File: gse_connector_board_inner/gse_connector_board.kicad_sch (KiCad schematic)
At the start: 27 parts, among them J1 arming_connector, J2 gse_com_connector, J3 chg_connector, J4 Conn_02x03_Top_Bottom, J5 Conn_02x02_Top_Bottom, U7 ISO1044BD, U9 MCP2562-E-SN

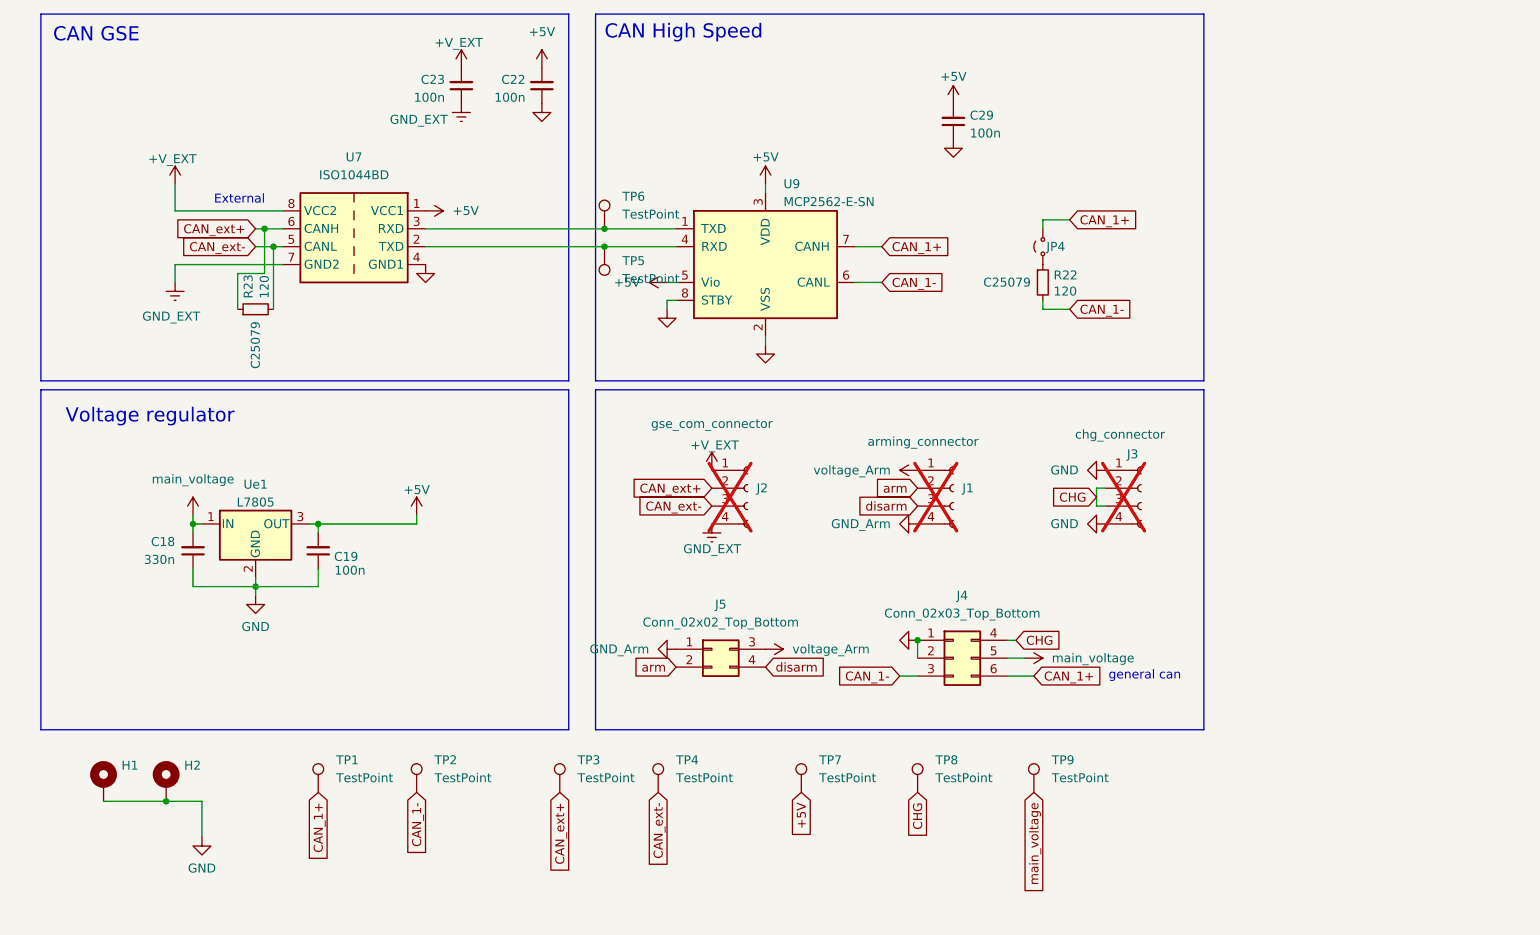
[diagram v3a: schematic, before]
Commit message: replace can isolation with mosfet
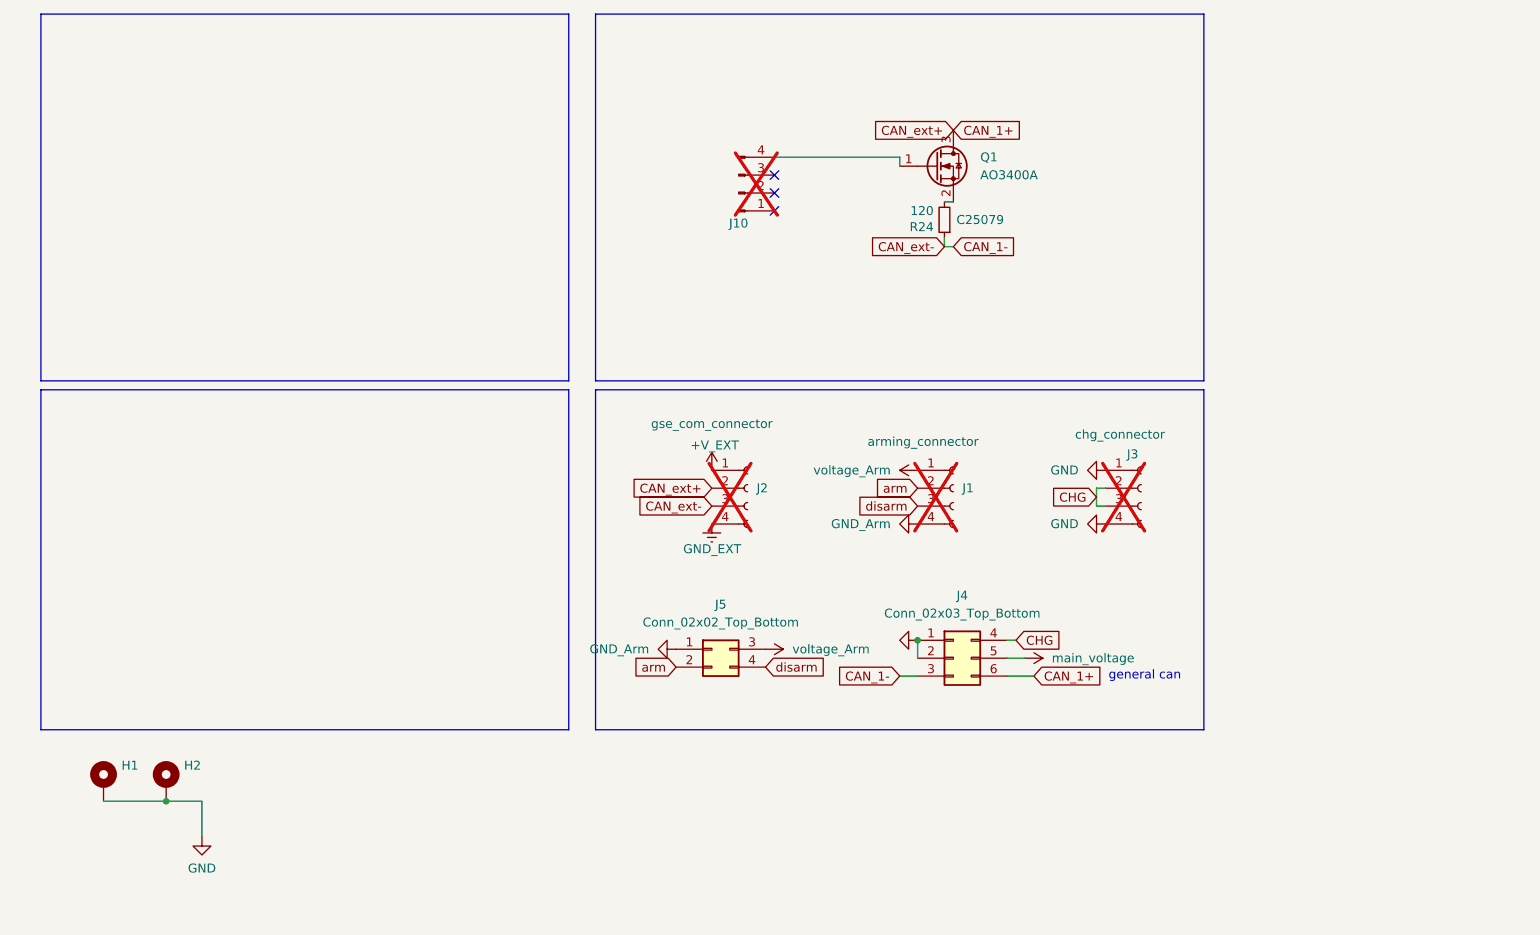
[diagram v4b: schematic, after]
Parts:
- removed C18: 330n, Capacitor_SMD:C_0603_1608Metric, symbol Device:C_Small
- removed C19: 100n, Capacitor_SMD:C_0603_1608Metric, symbol Device:C_Small
- removed C22, C23, C29: 100n, Capacitor_SMD:C_0603_1608Metric_Pad1.08x0.95mm_HandSolder, symbol Device:C_Small
- removed JP4: Jumper_2_Small_Open, Jumper:SolderJumper-2_P1.3mm_Bridged_RoundedPad1.0x1.5mm, symbol Jumper:Jumper_2_Small_Open
- removed R22, R23: 120, Resistor_SMD:R_0402_1005Metric, symbol Device:R_Small
- removed TP1, TP2, TP3, TP4, TP5, TP6, TP7, TP8, TP9: TestPoint, TestPoint:TestPoint_Pad_D1.5mm, symbol Connector:TestPoint
- removed U7: ISO1044BD, Package_SO:SOIC-8_3.9x4.9mm_P1.27mm, symbol Interface_CAN_LIN:ISO1044BD
- removed U9: MCP2562-E-SN, Package_SO:SOIC-8_3.9x4.9mm_P1.27mm, symbol Interface_CAN_LIN:MCP2562-E-SN
- removed Ue1: L7805, Package_TO_SOT_SMD:TO-252-2, symbol Regulator_Linear:L7805
- added J10: JST-GH 4Pin, Connector_JST:JST_GH_BM04B-GHS-TBT_1x04-1MP_P1.25mm_Vertical, symbol Connector:Conn_01x04_Pin
- added Q1: AO3400A, Package_TO_SOT_SMD:SOT-23, symbol Transistor_FET:AO3400A
- added R24: 120, Resistor_SMD:R_0402_1005Metric, symbol Device:R_Small
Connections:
- net CAN_ext+ is gone; now on net CAN_1+: J2.2 (Pin_2)
- net CAN_ext- is gone; now on net CAN_1-: J2.3 (Pin_3)
- net CAN_1+: now also Q1.3 (D)
- net CAN_1-: now also R24.1
- new net: Q1.2 (S), R24.2
- new net: J10.4 (Pin_4), Q1.1 (G)
- no-connect marks 0 -> 3
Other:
- note removed: "CAN GSE"
- note removed: "CAN High Speed"
- note removed: "External"
- note removed: "Voltage regulator"

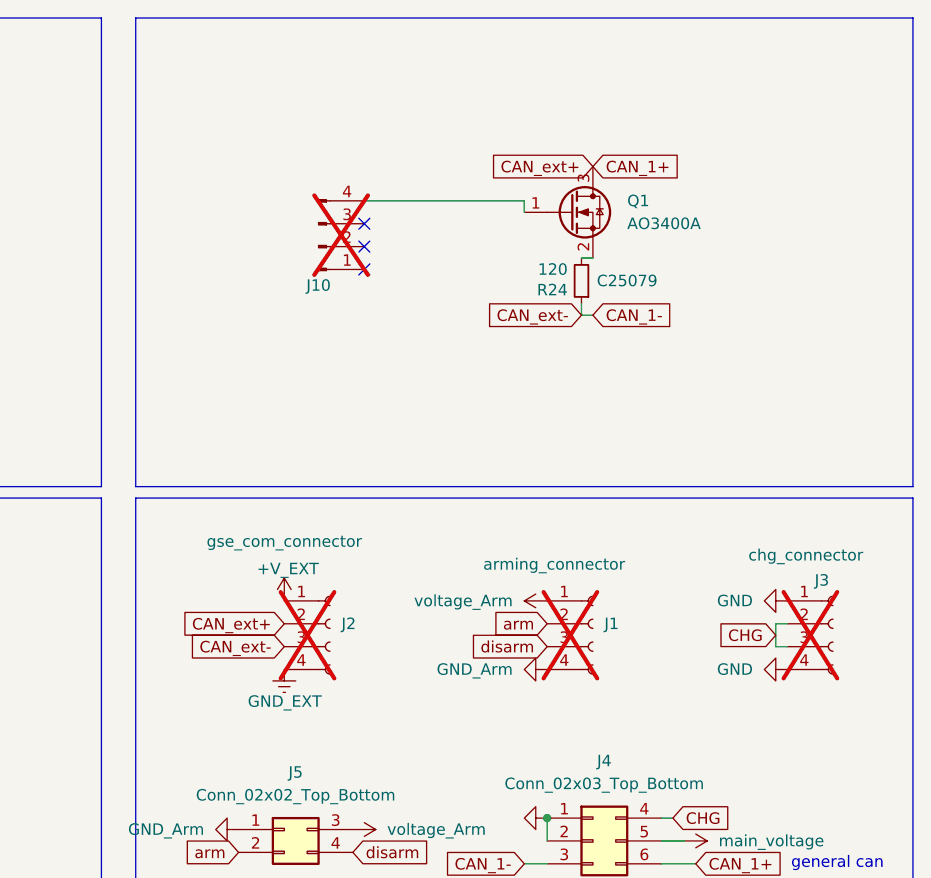
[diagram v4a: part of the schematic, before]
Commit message: replace can isolation with würth part
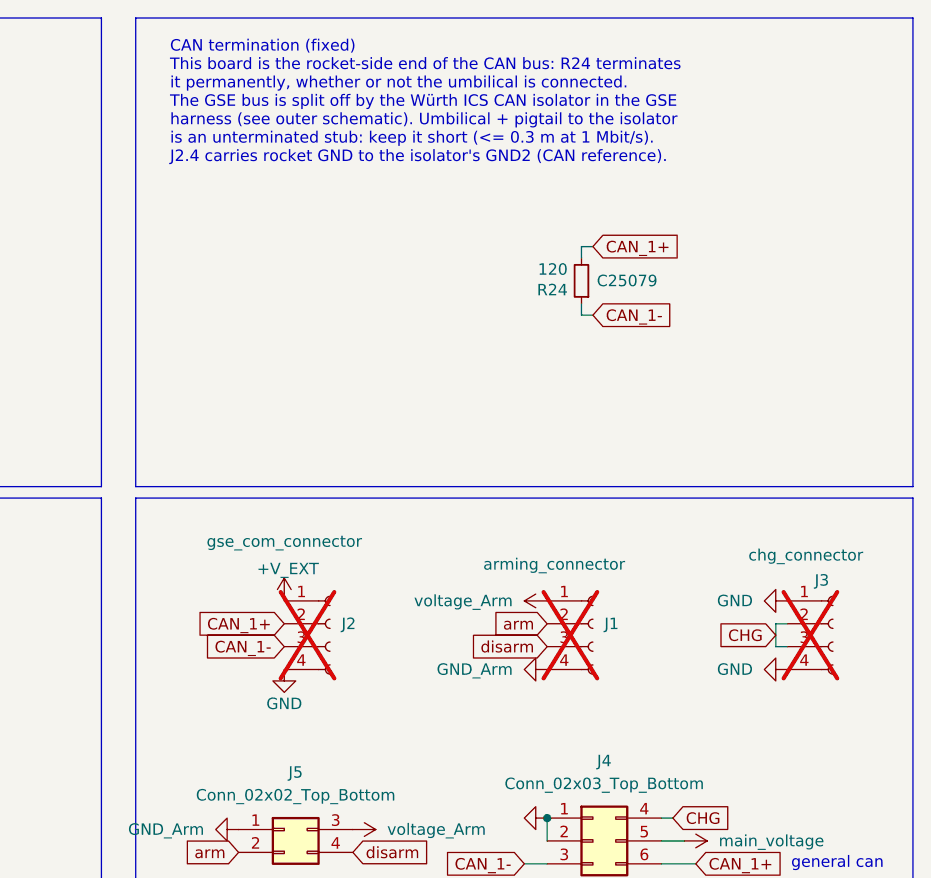
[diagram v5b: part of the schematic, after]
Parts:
- removed J10: JST-GH 4Pin, Connector_JST:JST_GH_BM04B-GHS-TBT_1x04-1MP_P1.25mm_Vertical, symbol Connector:Conn_01x04_Pin
- removed Q1: AO3400A, Package_TO_SOT_SMD:SOT-23, symbol Transistor_FET:AO3400A
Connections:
- net GND_EXT is gone; now on net GND: J2.4 (Pin_4)
- net CAN_1+: now also R24.2
- no-connect marks 3 -> 0
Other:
- note added: "CAN termination (fixed) This board is the rocket-side end of the CAN bus: R24 terminates it permanently, whether or not the umbilical is connected. The GSE bus is split off by the Würth ICS CAN isolator in the GSE harness (see outer schematic). Umbilical + pigtail to the isolator is an unterminated stub: keep it short (<= 0.3 m at 1 Mbit/s). J2.4 carries rocket GND to the isolator's GND2 (CAN ref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"

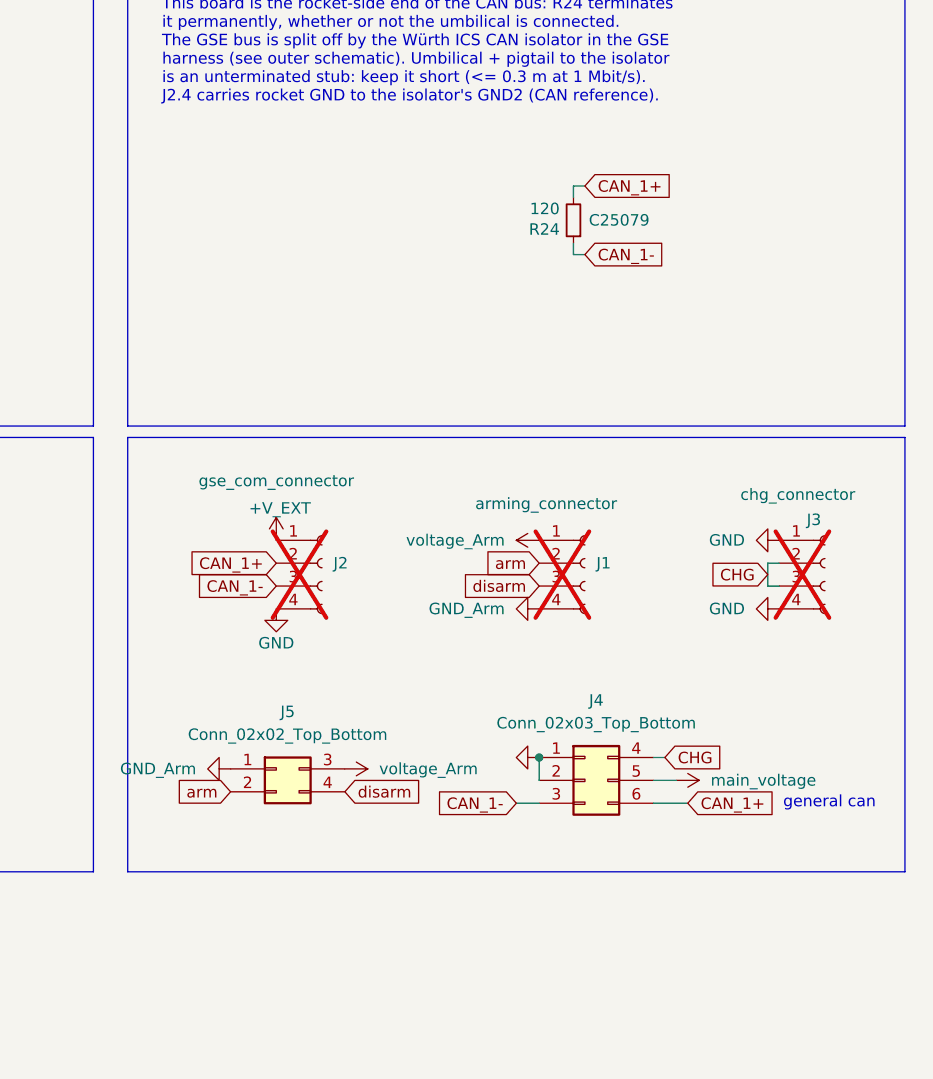
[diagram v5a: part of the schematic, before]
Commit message: add esd protection
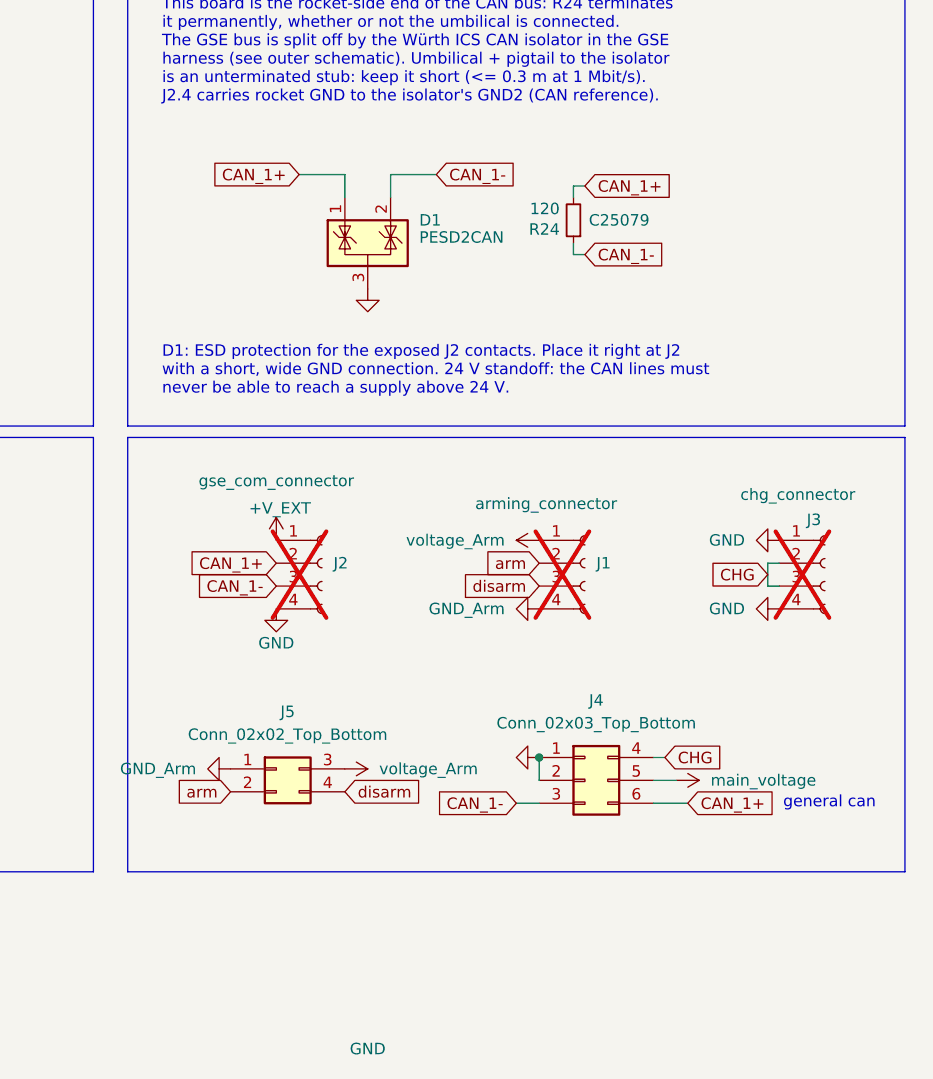
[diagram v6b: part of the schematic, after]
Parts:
- added D1: PESD2CAN, Package_TO_SOT_SMD:SOT-23, symbol Power_Protection:NUP2105L
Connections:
- net CAN_1+: now also D1.1 (K)
- net CAN_1-: now also D1.2 (K)
- net GND: now also D1.3 (A)
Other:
- note added: "D1: ESD protection for the exposed J2 contacts. Place it right at J2 with a short, wide GND connection. 24 V standoff: the CAN lines must never be able to reach a supply above 24 V."

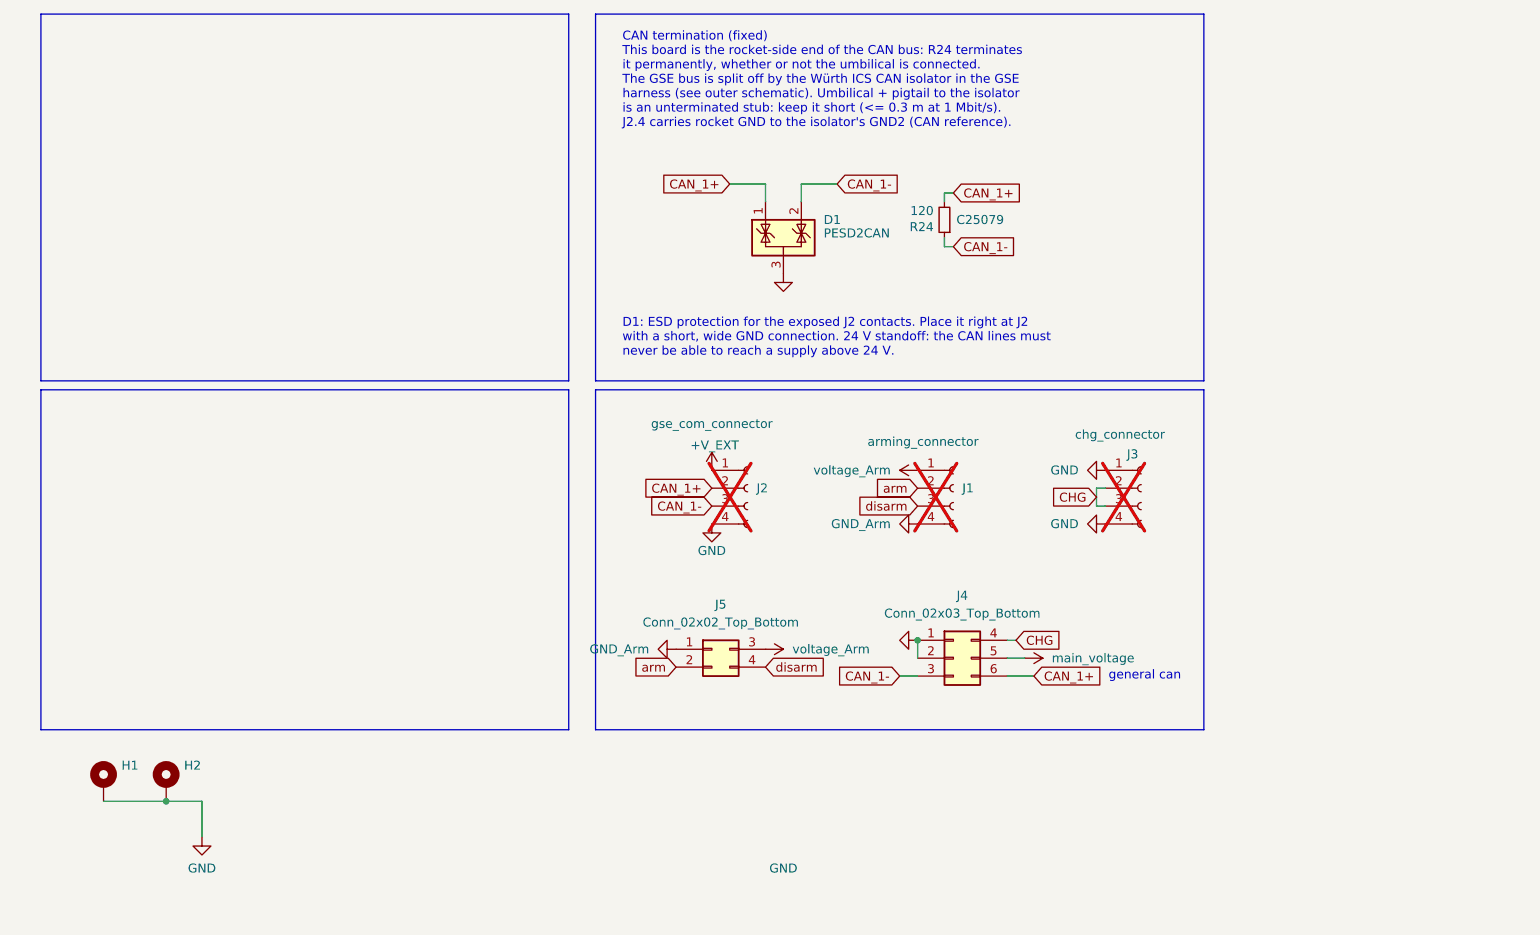
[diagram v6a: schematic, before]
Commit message: route new can isolation
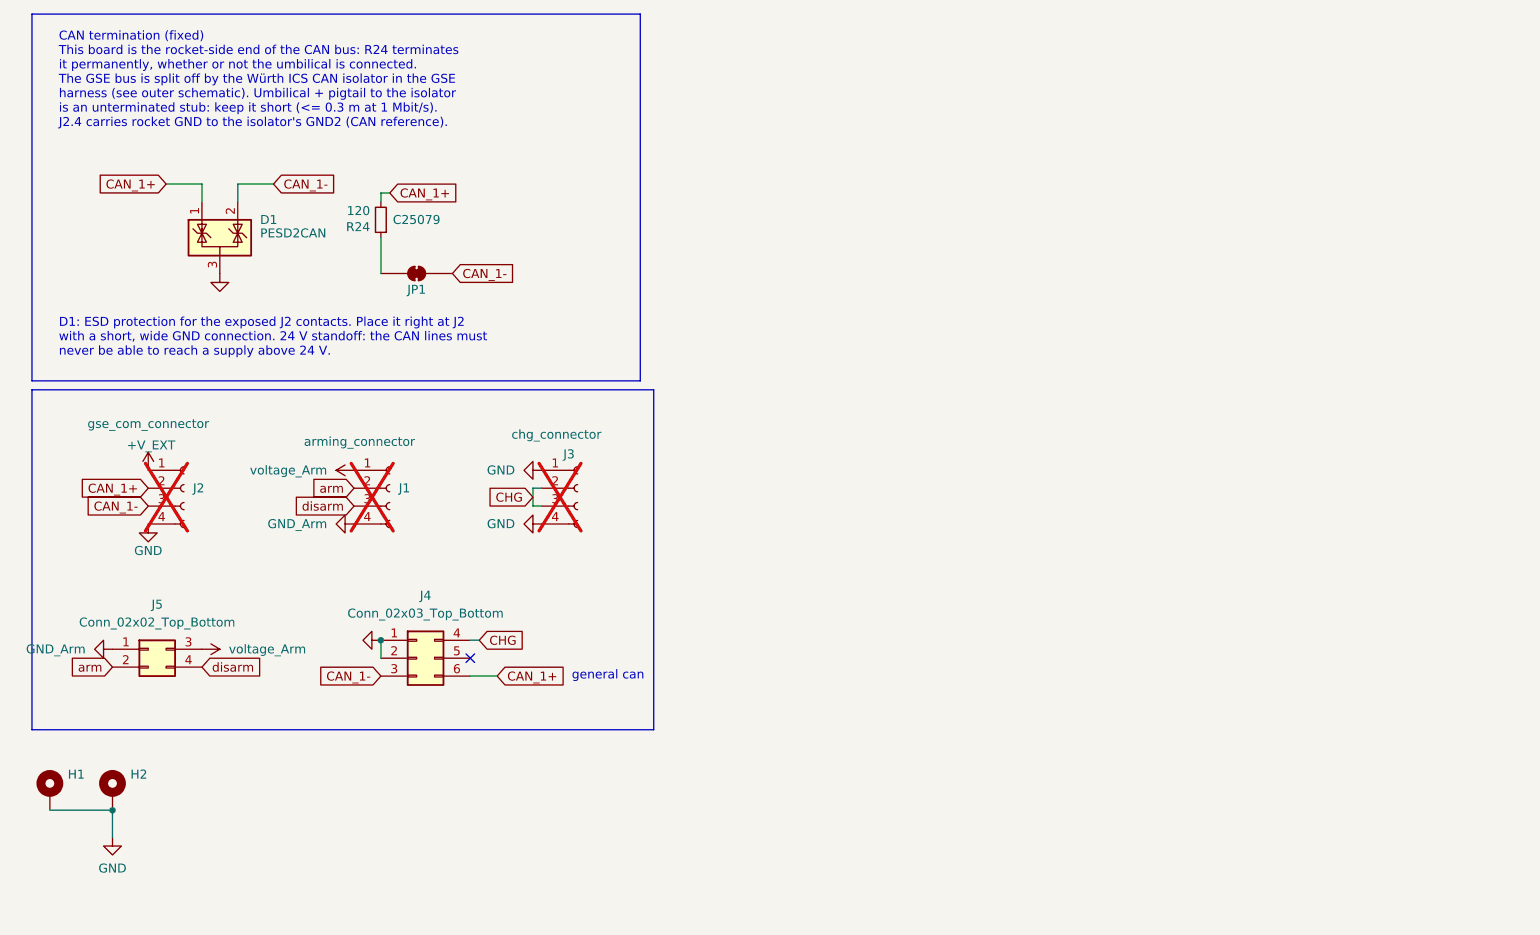
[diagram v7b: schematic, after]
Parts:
- added JP1: SolderJumper_2_Bridged, Jumper:SolderJumper-2_P1.3mm_Bridged_RoundedPad1.0x1.5mm, symbol Jumper:SolderJumper_2_Bridged
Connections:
- net CAN_1-: now also JP1.2 (B); no longer R24.1
- net main_voltage: no longer names the net of J4.5 (Pin_5)
- new net: JP1.1 (A), R24.1
- no-connect marks 0 -> 1
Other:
- moved on the sheet: D1, H1, H2, J1, J2, J3, J4, J5, R24
